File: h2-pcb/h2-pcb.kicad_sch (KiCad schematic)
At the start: 60 parts, among them J10 Temp Sensor Conn 3, J11 Actuator Connector 4, J12 Manometer Connector 3, J3 Manometer Connector 1, J4 Manometer Connector 2, J5 Actuator Connector 1, J6 Actuator Connector 2, J7 Actuator Connector 3, J8 Temp Sensor Conn 1, J9 Temp Sensor Conn 2, Q1 NMOS, Q2 PMOS, Q3 NMOS, Q4 PMOS, Q5 NMOS, Q6 PMOS, Q7 NMOS, Q8 PMOS, U4 DS2484R

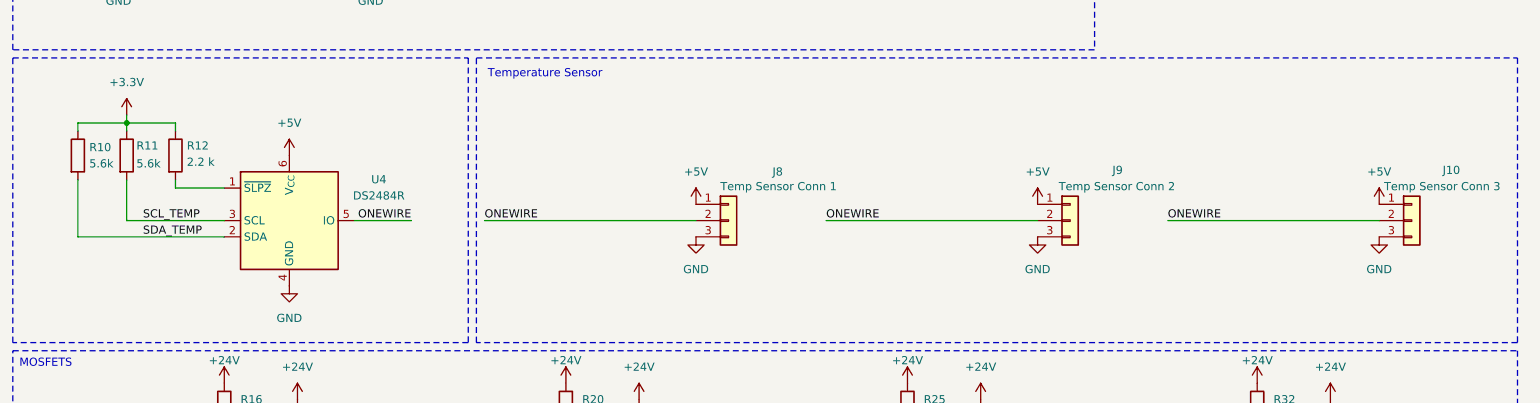
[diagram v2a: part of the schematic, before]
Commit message: h2-pcb: implement review comments
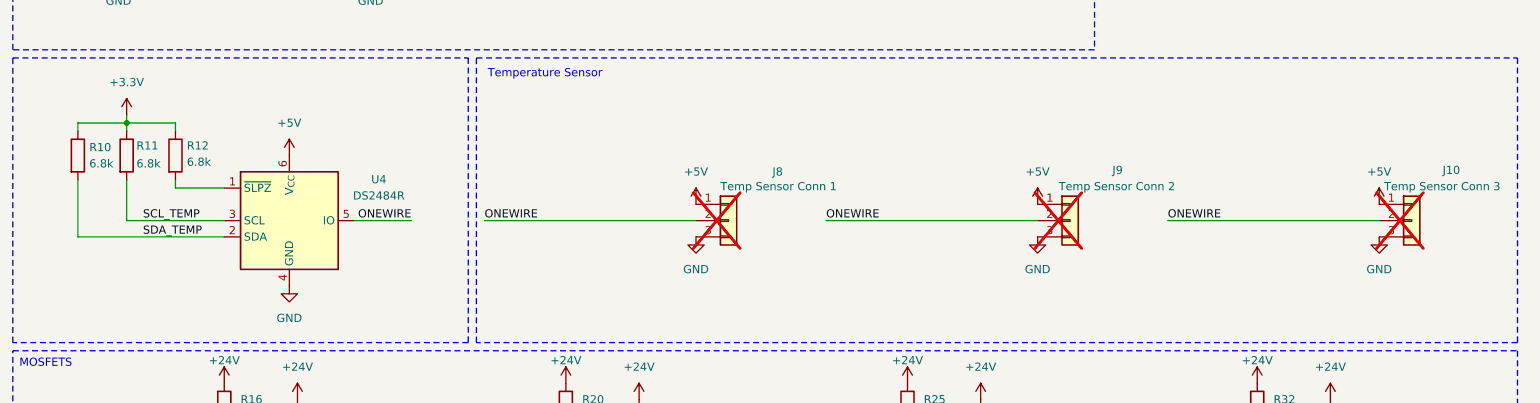
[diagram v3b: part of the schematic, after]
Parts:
- D3: footprint Exocet:LED_0805_2012Metric_With_Annotations -> LED_SMD:LED_0603_1608Metric
- J10, J8, J9: now not fitted
- R10, R11: value 5.6k -> 6.8k; footprint Resistor_SMD:R_0805_2012Metric -> Resistor_SMD:R_0603_1608Metric; JLCPCB C114627 -> C23212
- R12: value 2.2 k -> 6.8k; JLCPCB C113303 -> C23212
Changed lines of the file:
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@@
 		(in_bom yes)
 		(on_board yes)
-		(dnp no)
+		(dnp yes)
 		(property "Reference" "J9"
 			(at 185.674 214.376 0)
@@
 			)
 		)
-		(property "Footprint" "Exocet:LED_0805_2012Metric_With_Annotations"
+		(property "Footprint" "LED_SMD:LED_0603_1608Metric"
 			(at 328.93 105.41 0)
 			(effects
@@
 		(in_bom yes)
 		(on_board yes)
-		(dnp no)
+		(dnp yes)
 		(property "Reference" "J8"
 			(at 132.588 214.63 0)
@@
 		(in_bom yes)
 		(on_board yes)
-		(dnp no)
+		(dnp yes)
 		(property "Reference" "J10"
 			(at 237.236 214.376 0)
@@
 			)
 		)
-		(property "Value" "5.6k"
+		(property "Value" "6.8k"
 			(at 33.274 213.36 0)
 			(effects
@@
 			)
 		)
-		(property "Footprint" "Resistor_SMD:R_0805_2012Metric"
+		(property "Footprint" "Resistor_SMD:R_0603_1608Metric"
 			(at 29.972 212.09 90)
 			(effects
@@
 			)
 		)
-		(property "JLCPCB" "C114627"
+		(property "JLCPCB" "C23212"
 			(at 31.75 212.09 0)
 			(effects
@@
 			)
 		)
-		(property "Value" "2.2 k"
+		(property "Value" "6.8k"
 			(at 41.148 213.106 0)
 			(effects
@@
 			)
 		)
-		(property "JLCPCB" "C113303"
+		(property "JLCPCB" "C23212"
 			(at 39.37 212.09 0)
 			(effects
@@
 			)
 		)
-		(property "Value" "5.6k"
+		(property "Value" "6.8k"
 			(at 25.908 213.36 0)
 			(effects
@@
 			)
 		)
-		(property "Footprint" "Resistor_SMD:R_0805_2012Metric"
+		(property "Footprint" "Resistor_SMD:R_0603_1608Metric"
 			(at 22.352 212.09 90)
 			(effects
@@
 			)
 		)
-		(property "JLCPCB" "C114627"
+		(property "JLCPCB" "C23212"
 			(at 24.13 212.09 0)
 			(effects

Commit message: h2-pcb: Add 24V zone for connectors, change footprint for temp sensors + connect
Made 24V zone for right actuators connectors, network connector and 24V fuse holder.
Changed the temperature sensor connectors to JST_PH_S3B-PH-k_1x03_P2.00mm_Horizontal and placed them on the left side of pcb.
Followed with connecting the temperature sensors on the pcb.
TODO : fix 5 errors in DRC.
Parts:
- J10, J8, J9: footprint Connector_JST:JST_PH_B3B-PH-K_1x03_P2.00mm_Vertical -> Connector_JST:JST_PH_S3B-PH-K_1x03_P2.00mm_Horizontal
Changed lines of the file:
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@@
 			)
 		)
-		(property "Footprint" "Connector_JST:JST_PH_B3B-PH-K_1x03_P2.00mm_Vertical"
+		(property "Footprint" "Connector_JST:JST_PH_S3B-PH-K_1x03_P2.00mm_Horizontal"
 			(at 179.07 222.25 0)
 			(effects
@@
 			)
 		)
-		(property "Footprint" "Connector_JST:JST_PH_B3B-PH-K_1x03_P2.00mm_Vertical"
+		(property "Footprint" "Connector_JST:JST_PH_S3B-PH-K_1x03_P2.00mm_Horizontal"
 			(at 125.73 222.25 0)
 			(effects
@@
 			)
 		)
-		(property "Footprint" "Connector_JST:JST_PH_B3B-PH-K_1x03_P2.00mm_Vertical"
+		(property "Footprint" "Connector_JST:JST_PH_S3B-PH-K_1x03_P2.00mm_Horizontal"
 			(at 232.41 222.25 0)
 			(effects

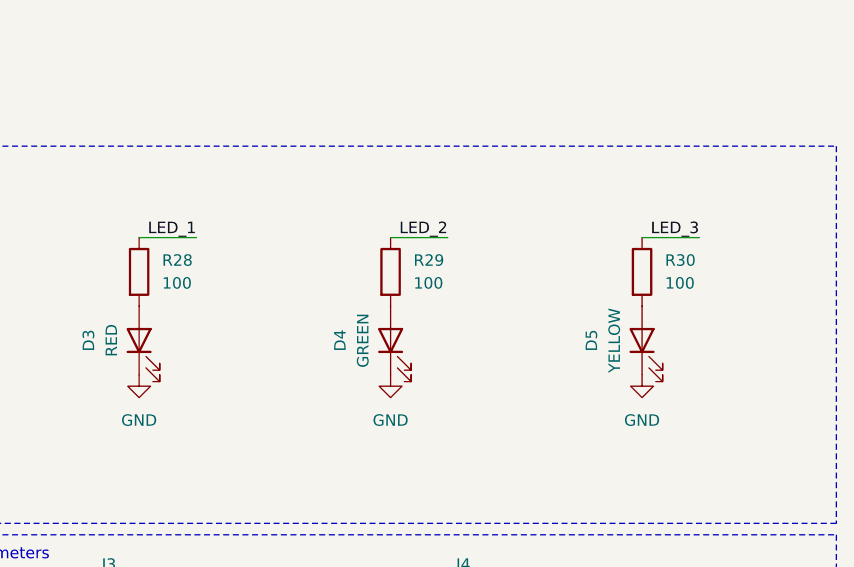
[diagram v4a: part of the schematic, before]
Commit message: h2-pcb: change value of LED resistors
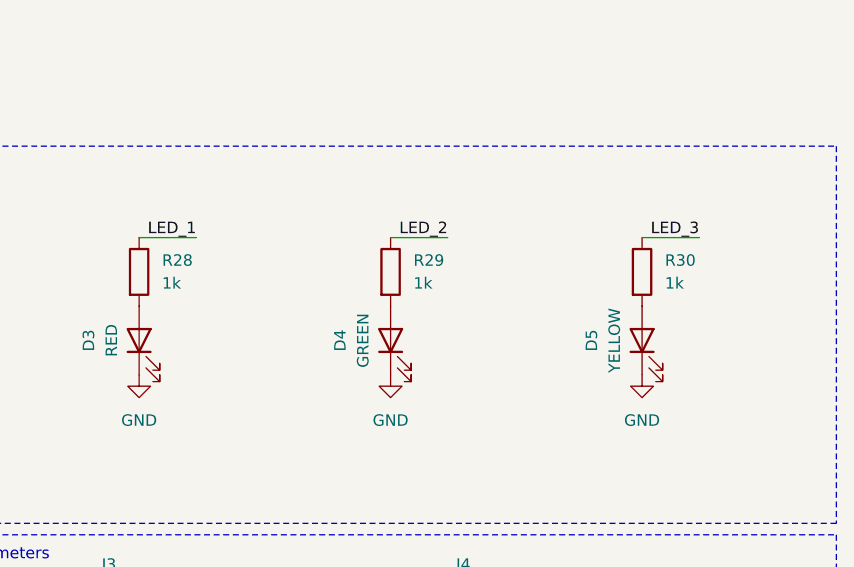
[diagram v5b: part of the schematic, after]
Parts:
- R28, R29, R30: value 100 -> 1k; JLCPCB C25076 -> C11702
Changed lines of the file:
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@@
 			)
 		)
-		(property "Value" "100"
+		(property "Value" "1k"
 			(at 387.35 99.0599 0)
 			(effects
@@
 			)
 		)
-		(property "JLCPCB" "C25076"
+		(property "JLCPCB" "C11702"
 			(at 384.81 97.79 0)
 			(effects
@@
 			)
 		)
-		(property "Value" "100"
+		(property "Value" "1k"
 			(at 359.41 99.0599 0)
 			(effects
@@
 			)
 		)
-		(property "JLCPCB" "C25076"
+		(property "JLCPCB" "C11702"
 			(at 356.87 97.79 0)
 			(effects
@@
 			)
 		)
-		(property "Value" "100"
+		(property "Value" "1k"
 			(at 331.47 99.0599 0)
 			(effects
@@
 			)
 		)
-		(property "JLCPCB" "C25076"
+		(property "JLCPCB" "C11702"
 			(at 328.93 97.79 0)
 			(effects

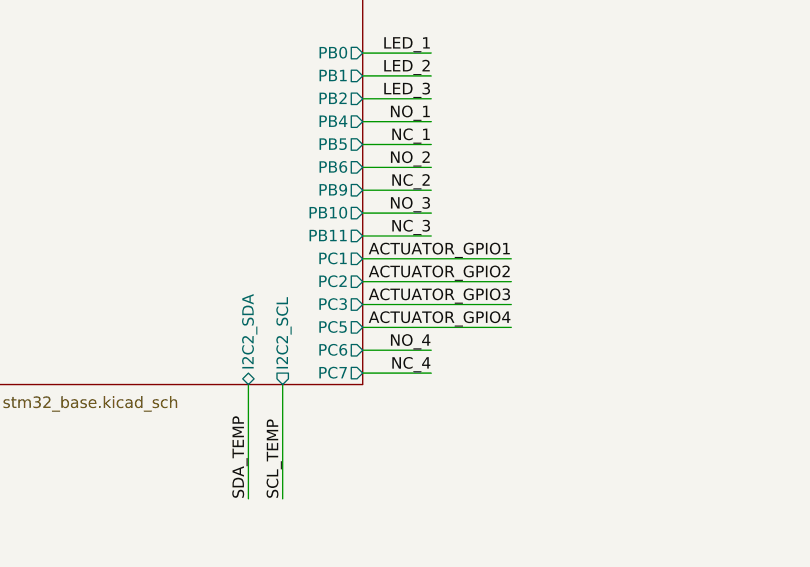
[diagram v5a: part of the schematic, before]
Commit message: h2-pcb: flip actuator connectors 3 & 4 to front layer
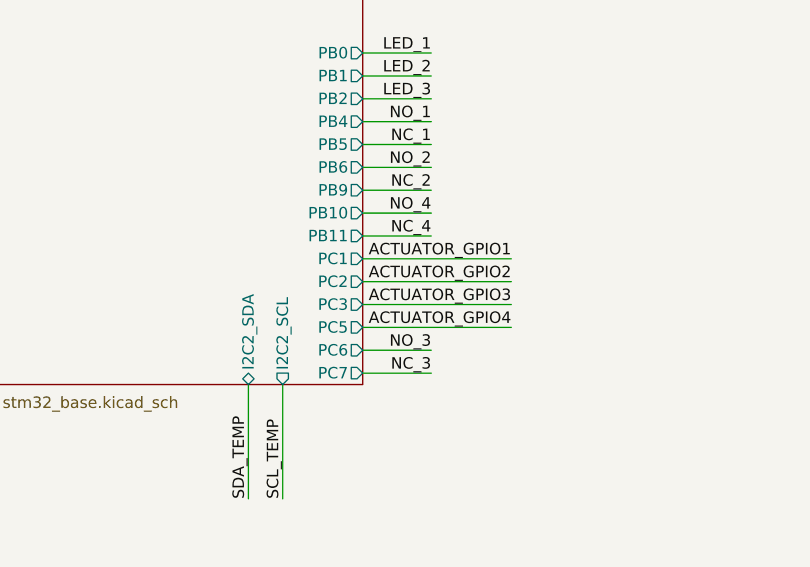
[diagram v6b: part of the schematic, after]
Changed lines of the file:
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@@
 		)
 	)
-	(label "NC_4"
+	(label "NC_3"
 		(at 66.04 66.04 180)
 		(effects
@@
 		)
 	)
-	(label "NO_3"
+	(label "NO_4"
 		(at 66.04 48.26 180)
 		(effects
@@
 		)
 	)
-	(label "NC_3"
+	(label "NC_4"
 		(at 66.04 50.8 180)
 		(effects
@@
 		)
 	)
-	(label "NO_4"
+	(label "NO_3"
 		(at 66.04 63.5 180)
 		(effects

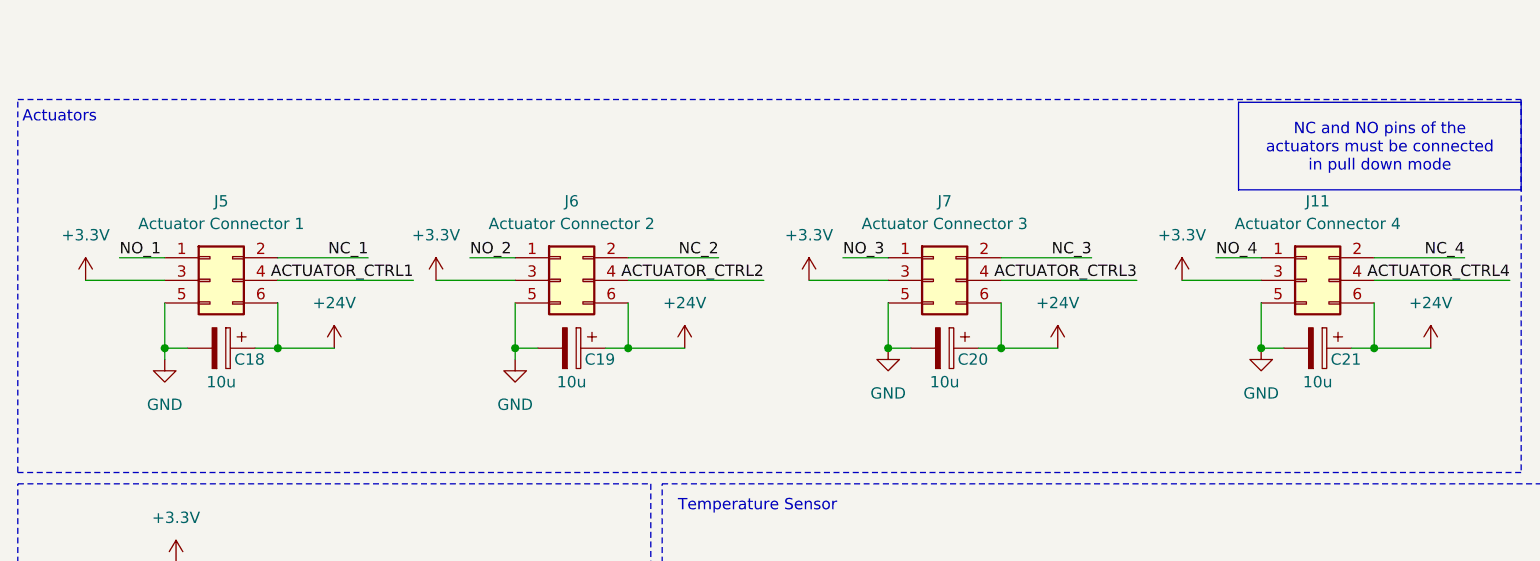
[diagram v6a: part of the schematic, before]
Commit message: h2-pcb: add DNP to actuator connectors
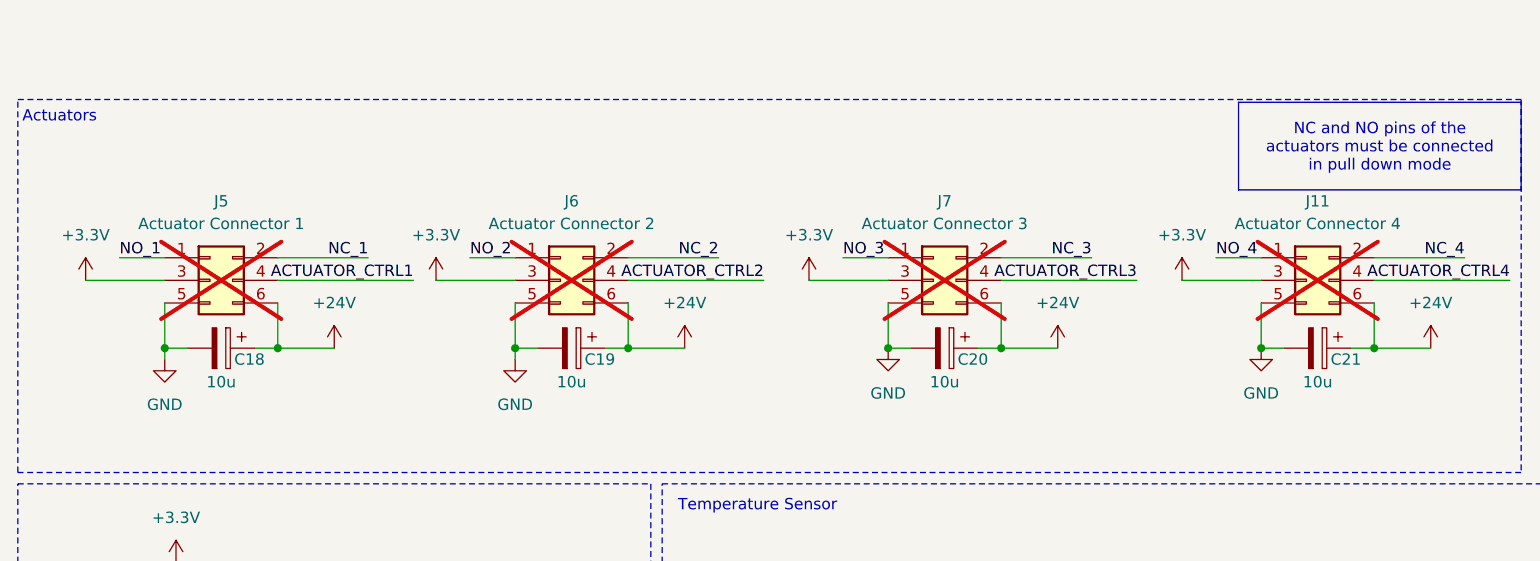
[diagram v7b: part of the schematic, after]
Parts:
- J11, J5, J6, J7: now not fitted
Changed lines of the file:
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@@
 		(in_bom yes)
 		(on_board yes)
-		(dnp no)
+		(dnp yes)
 		(fields_autoplaced yes)
 		(property "Reference" "J11"
@@
 		(in_bom yes)
 		(on_board yes)
-		(dnp no)
+		(dnp yes)
 		(fields_autoplaced yes)
 		(property "Reference" "J7"
@@
 		(in_bom yes)
 		(on_board yes)
-		(dnp no)
+		(dnp yes)
 		(fields_autoplaced yes)
 		(property "Reference" "J5"
@@
 		(in_bom yes)
 		(on_board yes)
-		(dnp no)
+		(dnp yes)
 		(fields_autoplaced yes)
 		(property "Reference" "J6"

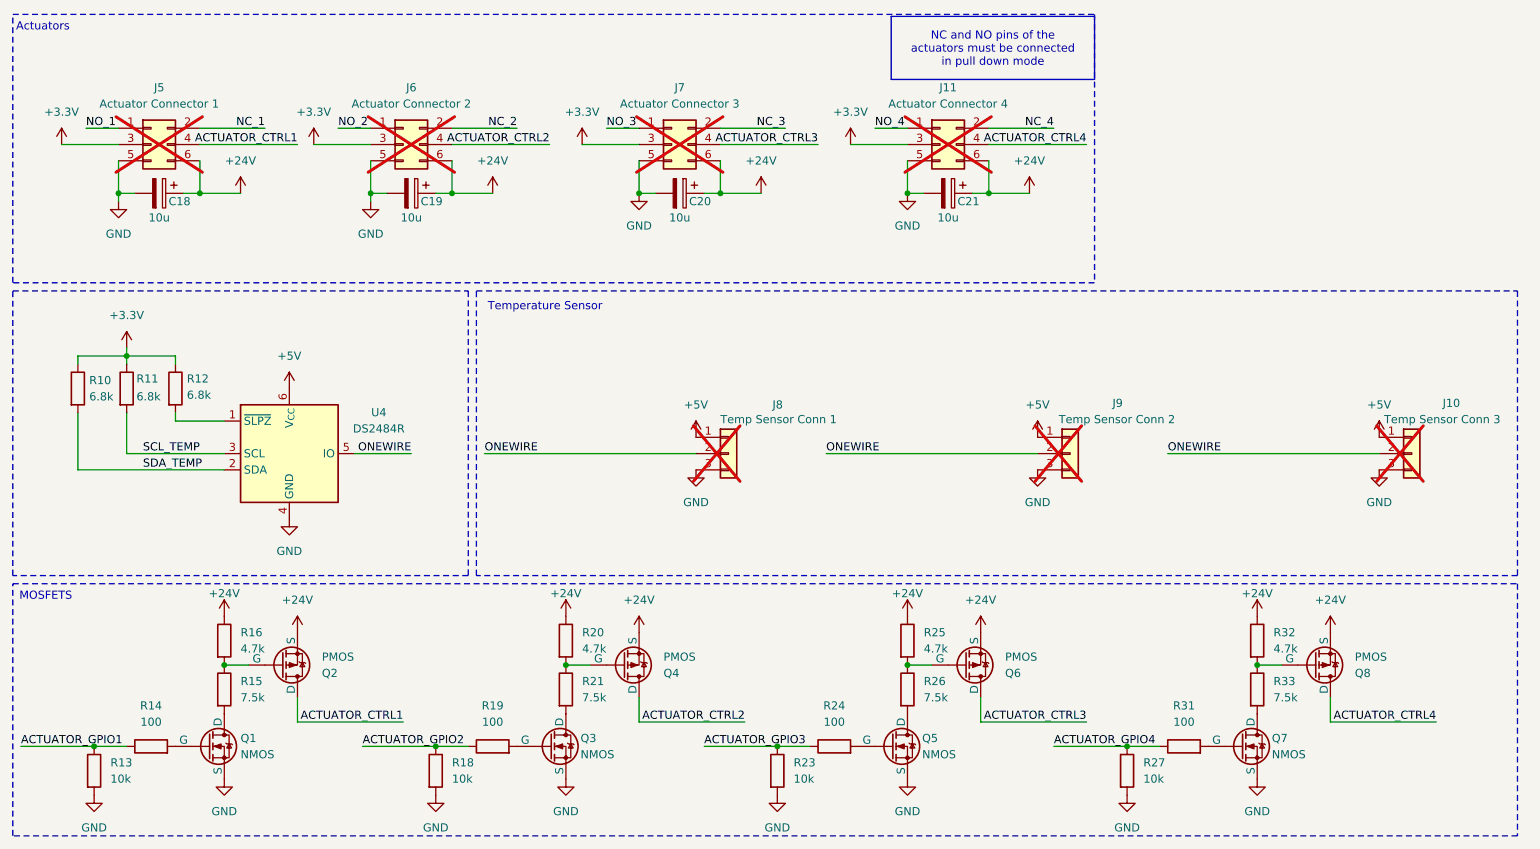
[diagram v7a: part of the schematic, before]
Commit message: h2-pcb: change MOSFET pins and part number
The orientation of the footprint did not match that of the actual
package. Also, the assembled parts have been changed.
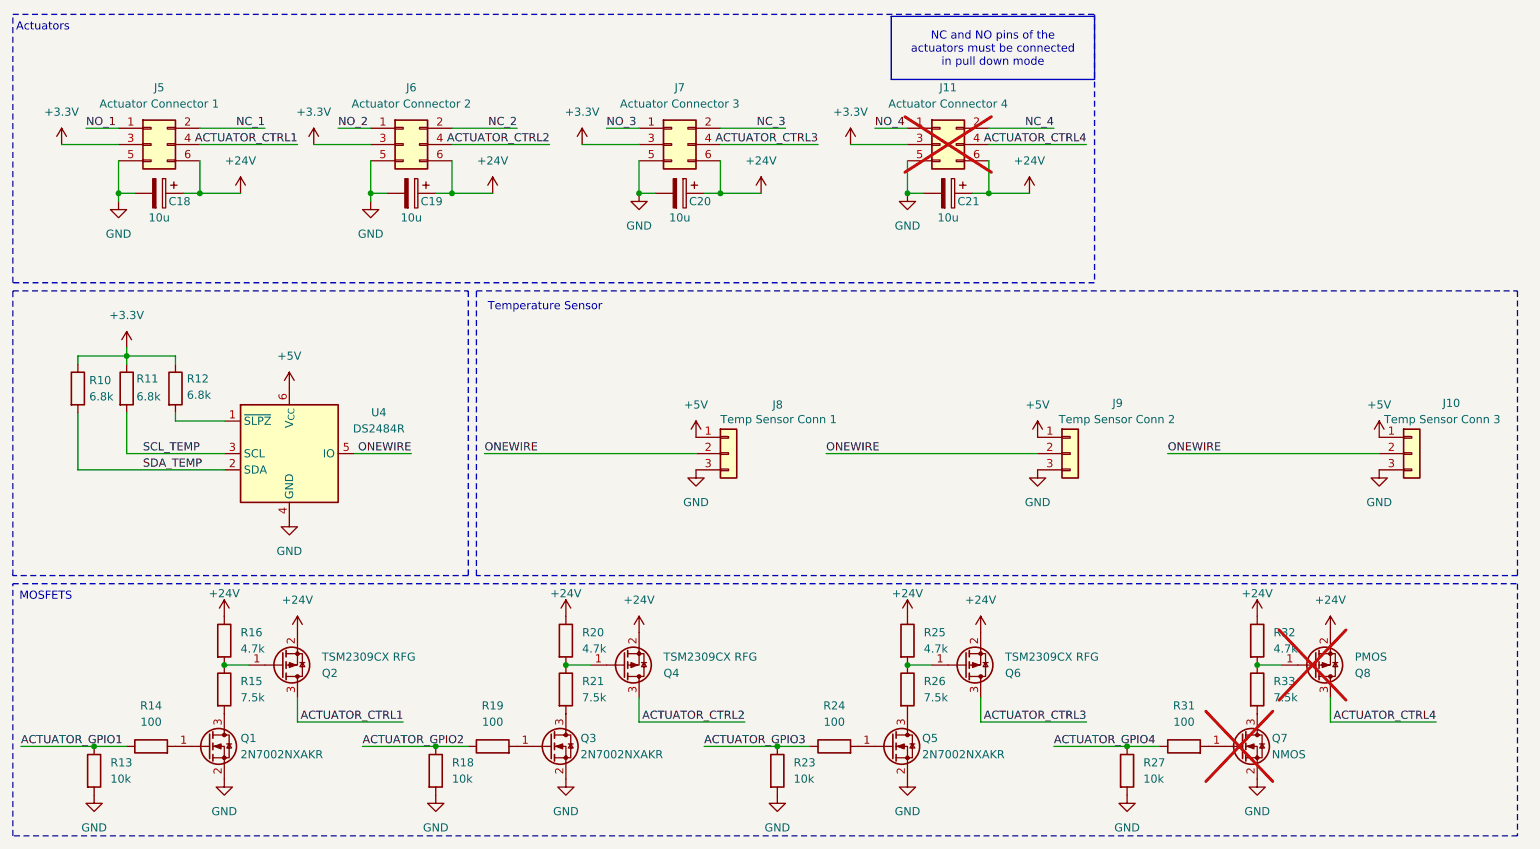
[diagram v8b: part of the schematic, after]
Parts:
- J10, J5, J6, J7, J8, J9: now fitted
- Q1, Q3, Q5: value NMOS -> 2N7002NXAKR; symbol Simulation_SPICE:NMOS -> Transistor_FET:Q_NMOS_GSD
- Q2, Q4, Q6: value PMOS -> TSM2309CX RFG; symbol Simulation_SPICE:PMOS -> Transistor_FET:Q_PMOS_GSD
- Q7: symbol Simulation_SPICE:NMOS -> Transistor_FET:Q_NMOS_GSD; now not fitted
- Q8: symbol Simulation_SPICE:PMOS -> Transistor_FET:Q_PMOS_GSD; now not fitted
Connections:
- net +24V: now also Q2.2 (S), Q4.2 (S), Q6.2 (S), Q8.2 (S); no longer Q2.3 (S), Q4.3 (S), Q6.3 (S), Q8.3 (S)
- net ACTUATOR_CTRL1: now also Q2.3 (D); no longer Q2.1 (D)
- net ACTUATOR_CTRL2: now also Q4.3 (D); no longer Q4.1 (D)
- net ACTUATOR_CTRL3: now also Q6.3 (D); no longer Q6.1 (D)
- net ACTUATOR_CTRL4: now also Q8.3 (D); no longer Q8.1 (D)
- net GND: now also Q1.2 (S), Q3.2 (S), Q5.2 (S), Q7.2 (S); no longer Q1.3 (S), Q3.3 (S), Q5.3 (S), Q7.3 (S)
- net at R15.1, R16.2: now also Q2.1 (G); no longer Q2.2 (G)
- net at R15.2: now also Q1.3 (D); no longer Q1.1 (D)
- net at Q3.1 (G): now also R19.2; no longer R21.2
- net at R25.2, R26.1: now also Q6.1 (G); no longer Q6.2 (G)
- net at R14.2: now also Q1.1 (G); no longer Q1.2 (G)
- net at R26.2: now also Q5.3 (D); no longer Q5.1 (D)
- net at R24.2: now also Q5.1 (G); no longer Q5.2 (G)
- net at R20.2, R21.1: now also Q4.1 (G); no longer Q4.2 (G)
- net at R32.2, R33.1: now also Q8.1 (G); no longer Q8.2 (G)
- net at R33.2: now also Q7.3 (D); no longer Q7.1 (D)
- net at R31.2: now also Q7.1 (G); no longer Q7.2 (G)
- new net: Q3.3 (D), R21.2
